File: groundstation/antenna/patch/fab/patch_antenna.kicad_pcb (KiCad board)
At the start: 2 copper layers, 160 x 160 mm, 0 parts

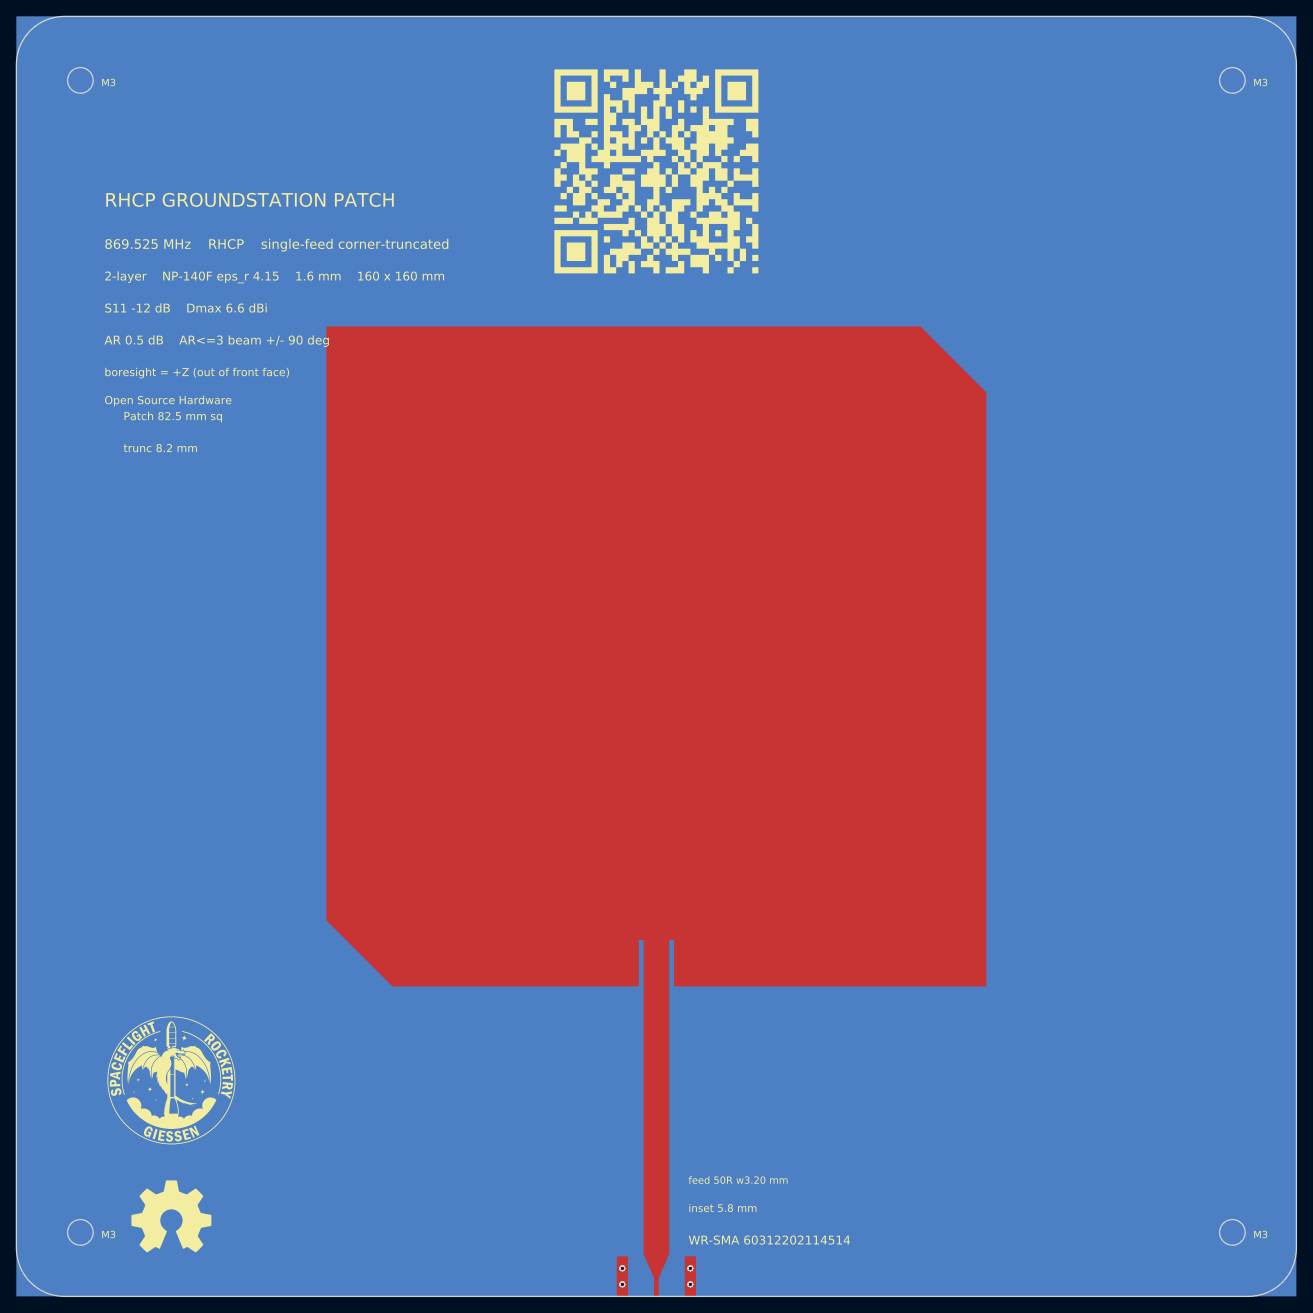
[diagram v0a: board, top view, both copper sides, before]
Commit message: Patch antenna: silk layout - QR right of patch, description top, logos centred-left; remove back graph + resistor text
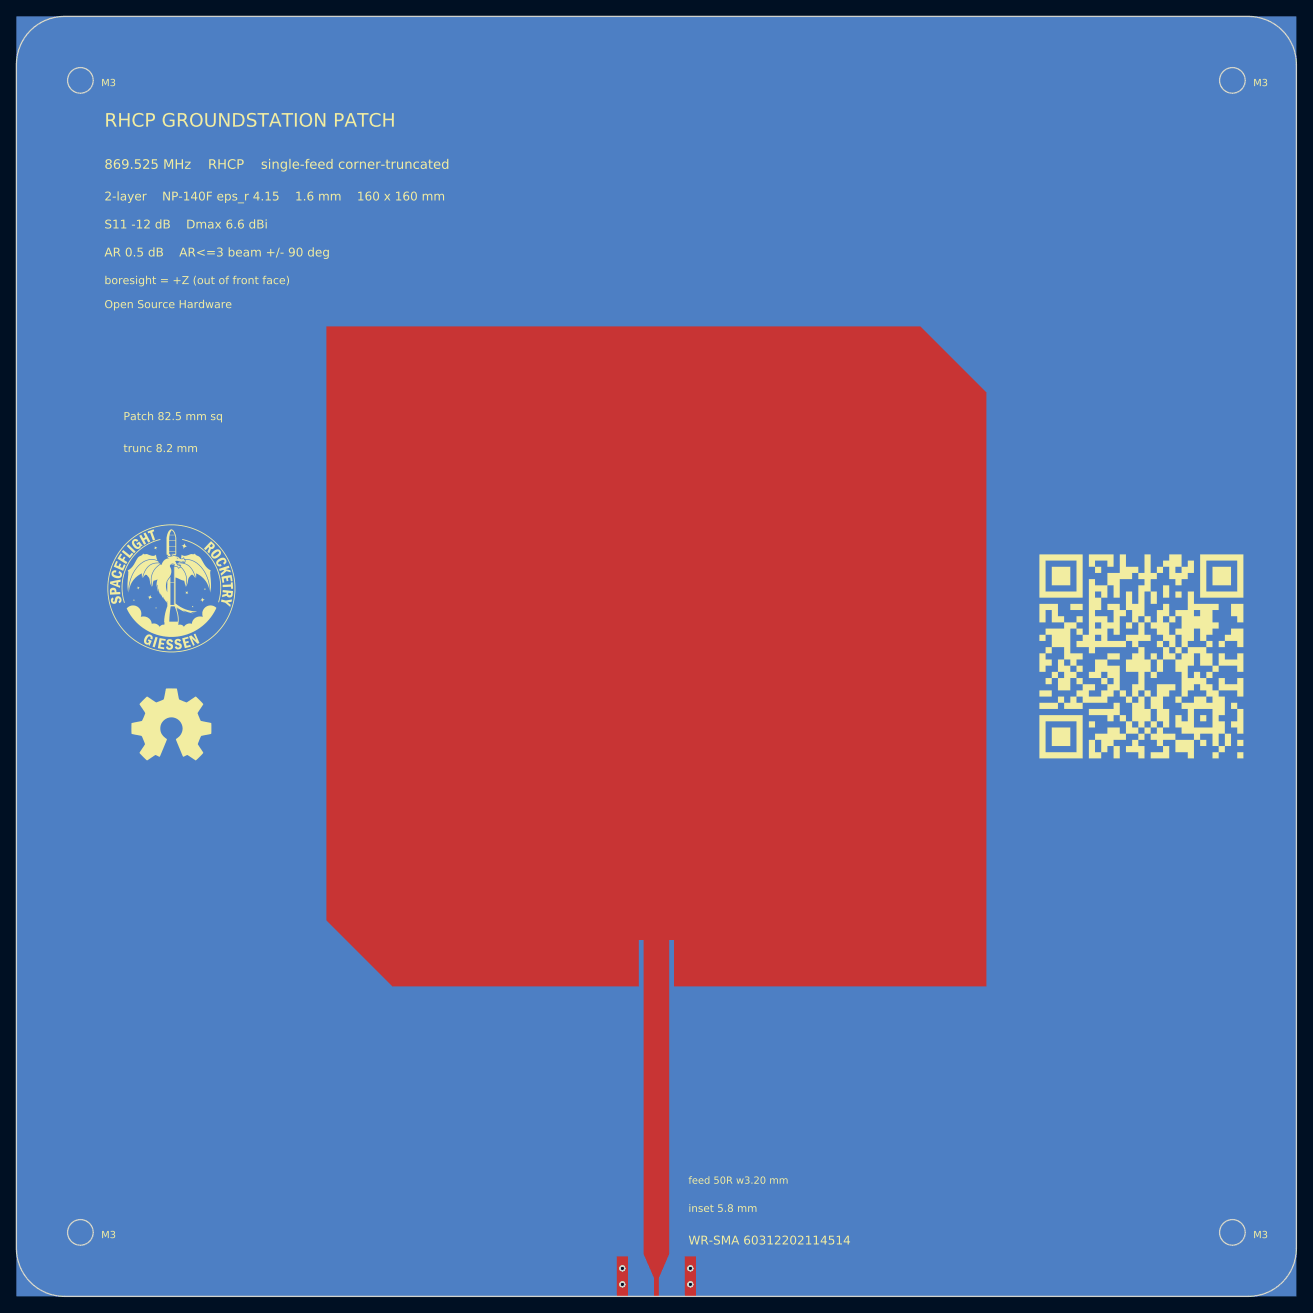
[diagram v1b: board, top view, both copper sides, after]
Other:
- board text added: "Hardware: edge-launch SMA (WE 60312202114514)"
- board text removed: "+90"
- board text removed: "-3 dB"
- board text removed: "-90"
- board text removed: "0"
- board text removed: "DIRECTIVITY (NF2FF); realised gain lower on FR-4-class"
- board text removed: "ELEVATION PATTERN"
- board text removed: "Hardware: edge-launch SMA (WE 60312202114514); no termination resistor"
- board text removed: "Method: openEMS FDTD @ 869.525 MHz"
- board text removed: "XZ cut phi = 0 (directivity)"
- board text removed: "boresight 6.6 dBi HPBW 91 deg (-46/+46) F/B 14 dB"
- board text removed: "theta (deg) - +Z boresight at centre"
